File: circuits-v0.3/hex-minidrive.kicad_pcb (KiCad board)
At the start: 4 copper layers, 18 x 48 mm, 81 parts, among them X1 16MHz

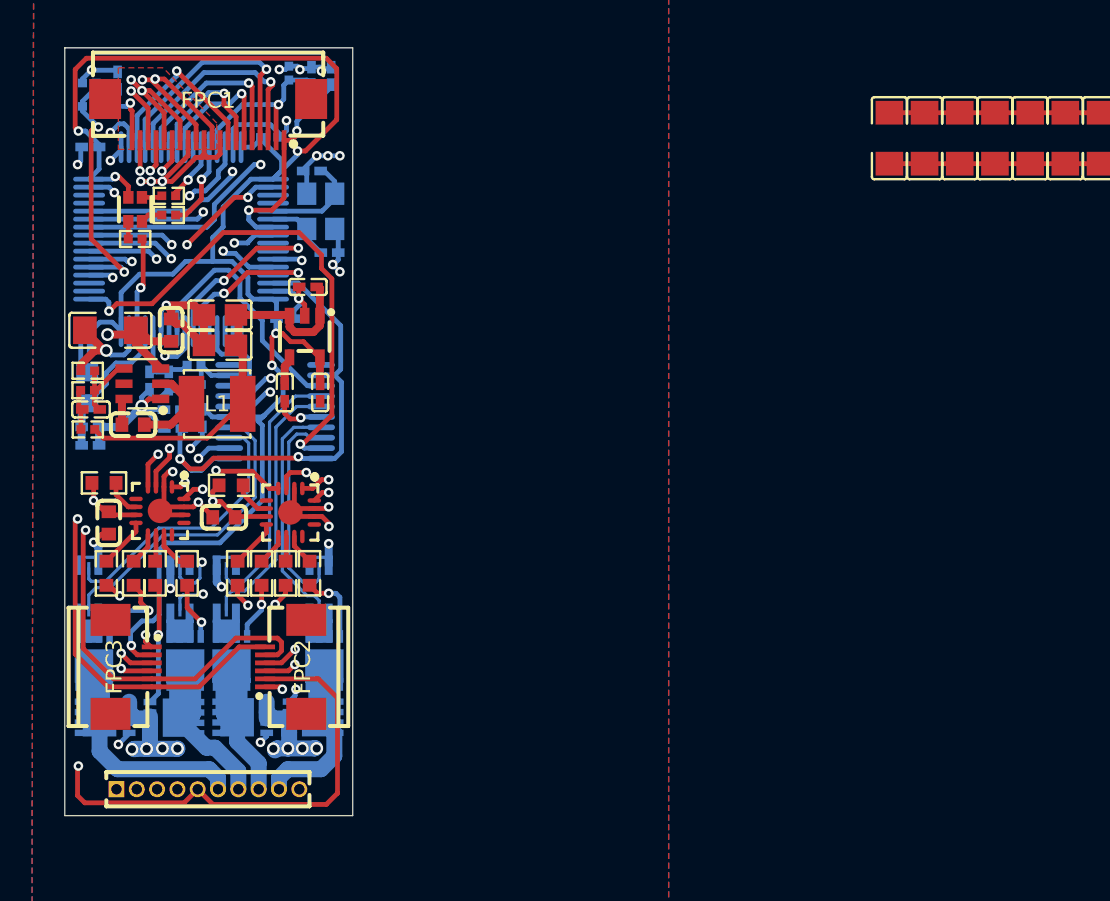
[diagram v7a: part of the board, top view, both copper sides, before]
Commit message: Thinned out the signal lines and tightened the layout, now to fit power caps.
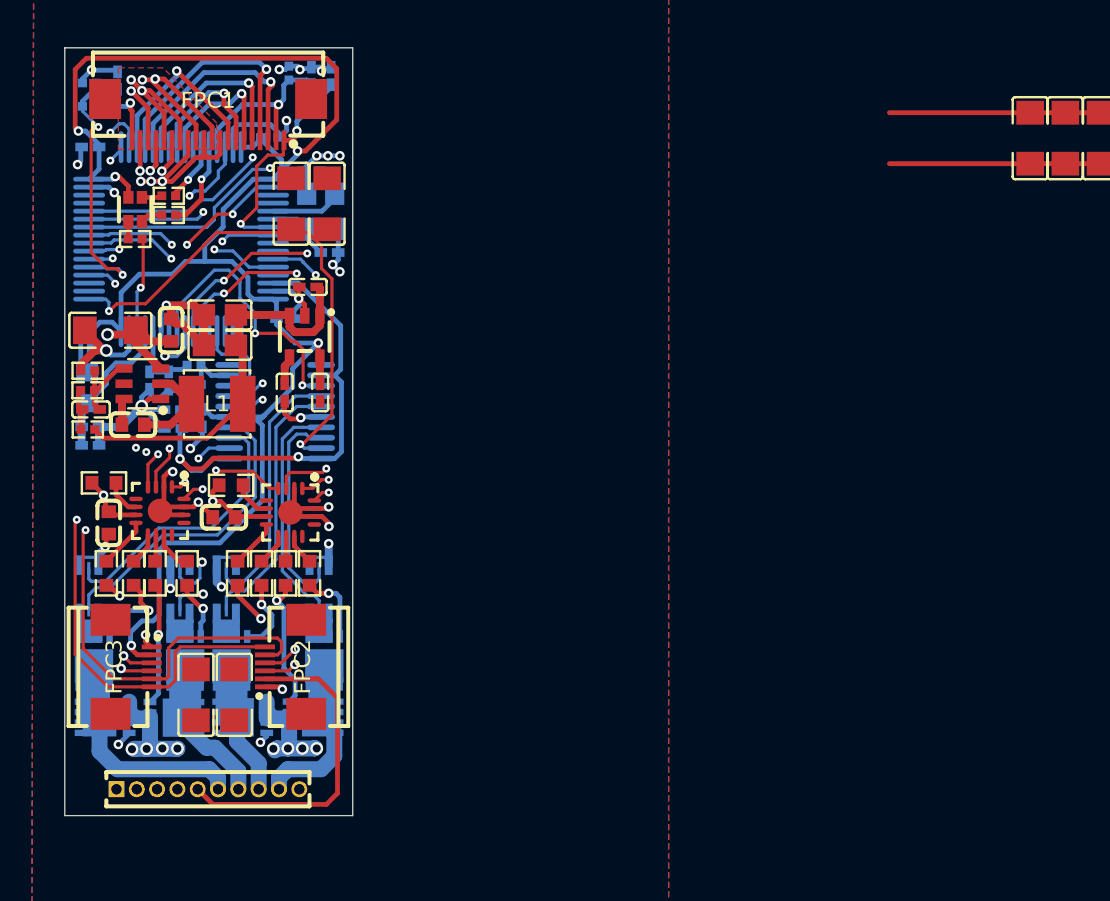
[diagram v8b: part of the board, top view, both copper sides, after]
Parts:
- moved C1 57.3 mm to (27.2, 60.5)
- moved C0 53.7 mm to (29.6, 60.5)
- moved C3 44.2 mm to (33.1, 29.8)
- moved C2 39.8 mm to (35.4, 29.8)
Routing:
- net 3V3: track 152.0 -> 148.1 mm, vias 7 -> 5
- net TIM3_CH2/ENCODER_2: track 41.9 -> 39.2 mm
- net TIM1_CH3: track 34.5 -> 36.8 mm
- net TIM3_CH1/ENCODER_1: track 39.3 -> 37.1 mm
- net /Gate-1-Positive: track 12.3 -> 14.4 mm
- net -Probe-2: track 20.0 -> 18.3 mm
- net +Probe-2: track 20.0 -> 18.3 mm
- net TIM1_CH3N: track 29.6 -> 28.1 mm
- net TIM1_CH2: track 30.3 -> 28.8 mm
- net ADC1_IN12/M3_CURRENT: track 15.8 -> 17.2 mm, vias 0 -> 2
- net SYS_JTMS-SVDIO: track 48.6 -> 49.7 mm
- net /Gate-3-Negative: track 3.57 -> 4.64 mm
- net SYS_JTCK-SWCLK: track 50.1 -> 51.2 mm
- net NRST: track 13.4 -> 14.0 mm
- net TIM1_CH1: track 20.0 -> 20.5 mm
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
